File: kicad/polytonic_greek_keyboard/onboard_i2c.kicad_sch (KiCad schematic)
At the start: 13 parts, among them Q1 S8050, U2 PCF8574T

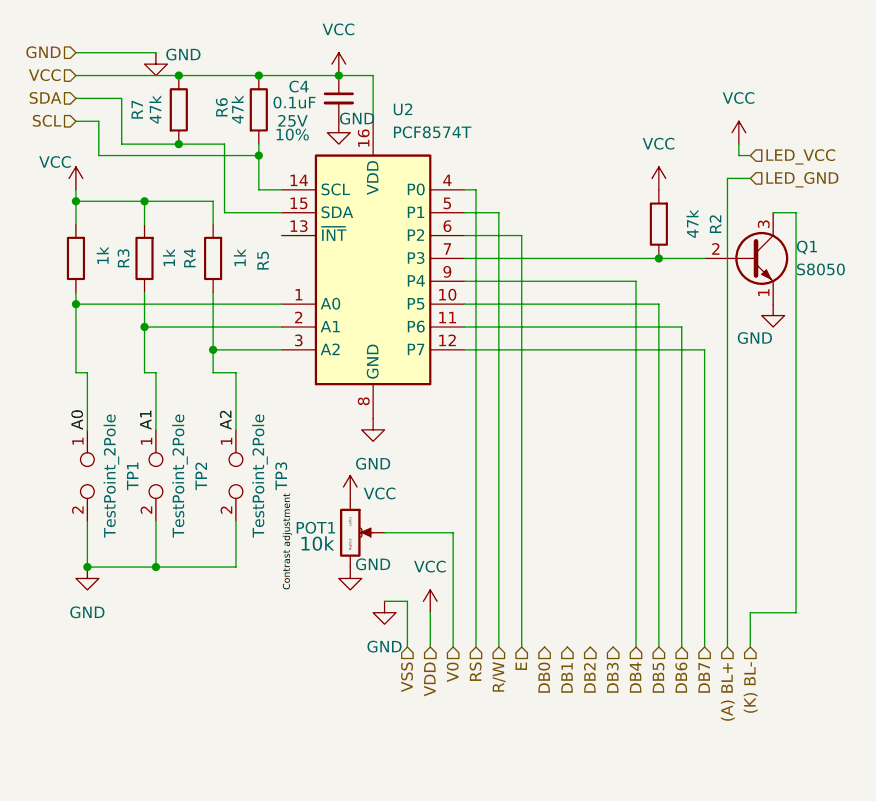
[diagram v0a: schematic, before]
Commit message: [ADD] a more structured approach of the pcb in a way that won't overload the esp32 that is running it
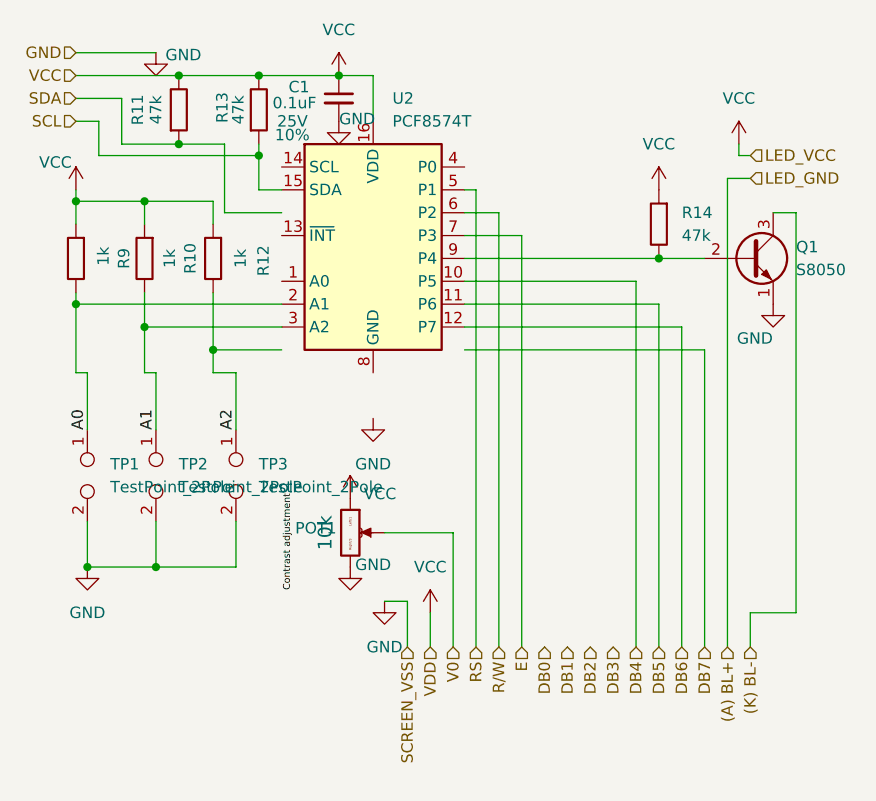
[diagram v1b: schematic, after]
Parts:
- POT1: footprint PCM_Potentiometer_THT_US_AKL:Potentiometer_Alps_RK09L_Single_Vertical -> Misc:Potentiometer_Piher_PC-16_Single_Vertical
- TP1, TP2, TP3: footprint Pin_Headers:Pin_Header_Straight_2x01_Pitch2.00mm_SMD -> Misc:TestPoint_2Pads_Pitch5.08mm_Drill1.3mm
- renumbered C4 to C1, R4 to R10, R7 to R11, R5 to R12, R6 to R13, R2 to R14, R3 to R9
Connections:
- net A0: now also U2.2 (A1); no longer U2.1 (A0)
- net A1: now also U2.3 (A2); no longer U2.2 (A1)
- net A2: no longer U2.3 (A2)
- net DB4: now also U2.10 (P5); no longer U2.9 (P4)
- net DB5: now also U2.11 (P6); no longer U2.10 (P5)
- net DB6: now also U2.12 (P7); no longer U2.11 (P6)
- net DB7: no longer U2.12 (P7)
- net E: now also U2.7 (P3); no longer U2.6 (P2)
- net GND: no longer U2.8 (GND)
- net RS: now also U2.5 (P1); no longer U2.4 (P0)
- net R/W: now also U2.6 (P2); no longer U2.5 (P1)
- net SCL: now also U2.15 (SDA); no longer U2.14 (SCL)
- net SDA: no longer U2.15 (SDA)
- net at Q1.2 (B), R14.2: now also U2.9 (P4); no longer U2.7 (P3)
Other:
- moved on the sheet: U2

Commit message: [UPDATE] the board desing, [FIX] connection issues
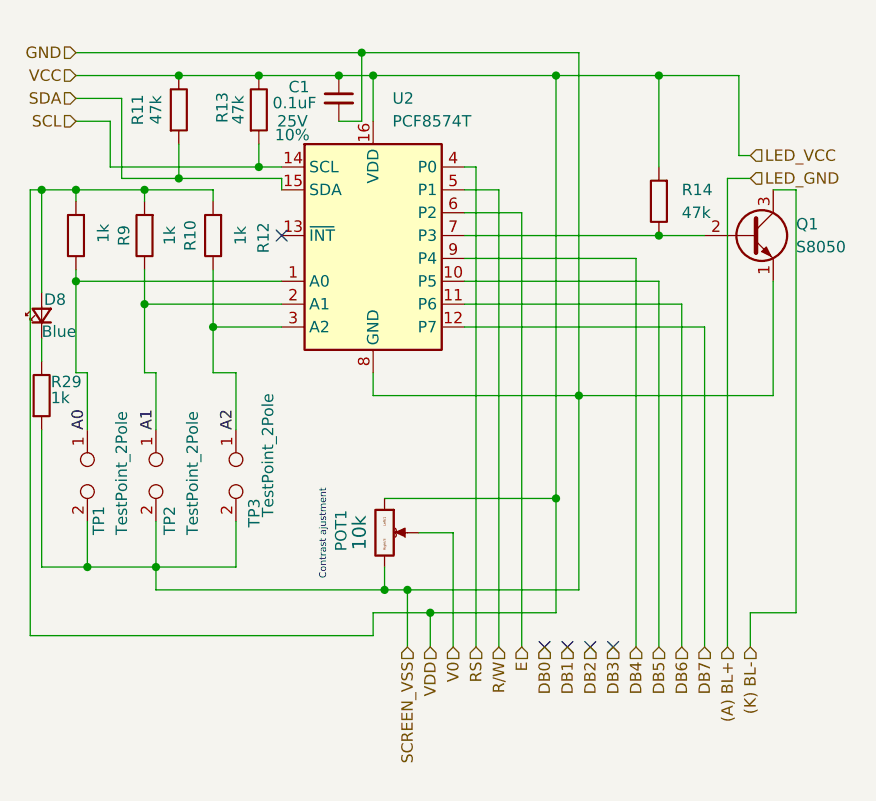
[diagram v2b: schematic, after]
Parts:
- added D8: Blue, PCM_SparkFun-LED:LED_1206_3216Metric_Blue, symbol PCM_SparkFun-LED:LED_Blue_1206
- added R29: 1k, Resistor_THT:R_Axial_DIN0207_L6.3mm_D2.5mm_P10.16mm_Horizontal, symbol PCM_SL_Resistors:1k
- POT1: footprint Misc:Potentiometer_Piher_PC-16_Single_Vertical -> Misc:Potentiometer_TT_P0915N
- TP1, TP2, TP3: footprint Misc:TestPoint_2Pads_Pitch5.08mm_Drill1.3mm -> Connector_PinHeader_2.00mm:PinHeader_1x02_P2.00mm_Horizontal
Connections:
- net A0: now also U2.1 (A0); no longer U2.2 (A1)
- net A1: now also U2.2 (A1); no longer U2.3 (A2)
- net A2: now also U2.3 (A2)
- net DB4: now also U2.9 (P4); no longer U2.10 (P5)
- net DB5: now also U2.10 (P5); no longer U2.11 (P6)
- net DB6: now also U2.11 (P6); no longer U2.12 (P7)
- net DB7: now also U2.12 (P7)
- net E: now also U2.6 (P2); no longer U2.7 (P3)
- net GND: now also U2.8 (GND), R29.1
- net RS: now also U2.4 (P0); no longer U2.5 (P1)
- net R/W: now also U2.5 (P1); no longer U2.6 (P2)
- net SCL: now also U2.14 (SCL); no longer U2.15 (SDA)
- net SDA: now also U2.15 (SDA)
- net at Q1.2 (B), R14.2: now also U2.7 (P3); no longer U2.9 (P4)
- net VCC renamed LED_VCC
- net LED_VCC: now also D8.2 (A)
- new net: D8.1 (K), R29.2
- no-connect marks 0 -> 5
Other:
- note added: "Contrast ajustment"
- moved on the sheet: POT1, Q1, R10, R12, R14, R9

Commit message: [UPDATE] the desing to fit on two separate pcbs
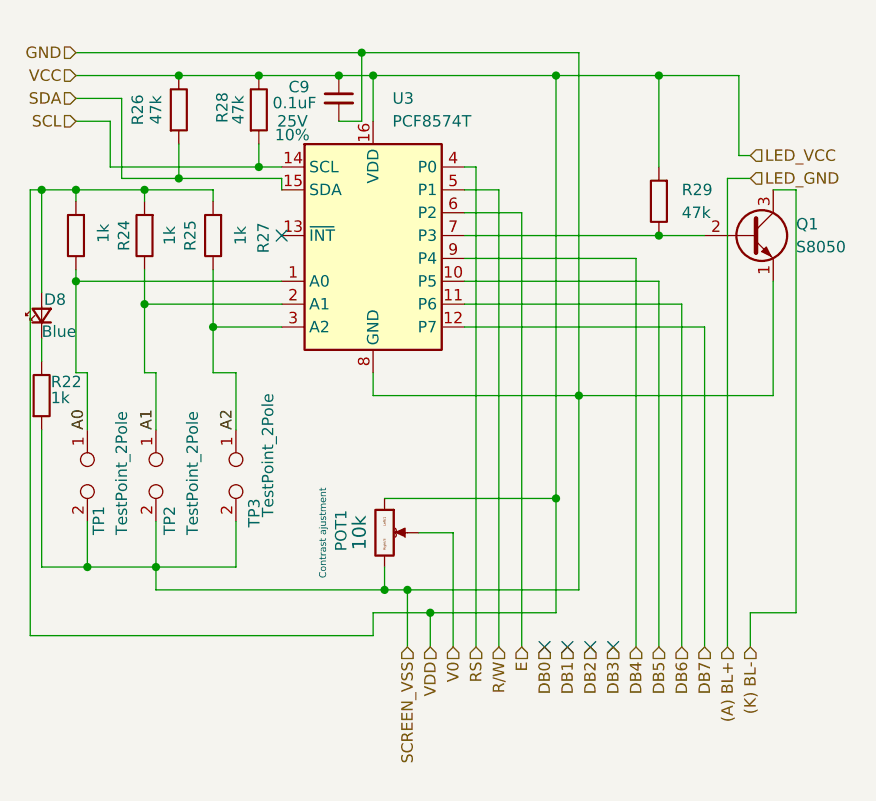
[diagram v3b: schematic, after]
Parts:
- renumbered C1 to C9, R29 to R22, R9 to R24, R10 to R25, R11 to R26, R12 to R27, R13 to R28, R14 to R29, U2 to U3
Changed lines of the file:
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@@
 		)
 		(instances
-			(project ""
-				(path "/cbe25a1b-6c02-43c2-9ff9-ba274c7cf6a2/b9347469-4bb2-4648-b4dc-d6f3187000d0/79c338a4-4a9b-4797-93e1-f6bef1aecfbc"
+			(project "polytonic_greek_keyboard"
+				(path "/cbe25a1b-6c02-43c2-9ff9-ba274c7cf6a2/8498b325-11fd-4b20-a704-75ec3d8987ef/ec54e47a-8e8b-4416-b579-fc6e7c329b94/79c338a4-4a9b-4797-93e1-f6bef1aecfbc"
 					(reference "POT1")
 					(unit 1)
@@
 		(on_board yes)
 		(dnp no)
-		(property "Reference" "C1"
+		(property "Reference" "C9"
 			(at 42.672 17.78 0)
 			(effects
@@
 		)
 		(instances
-			(project ""
-				(path "/cbe25a1b-6c02-43c2-9ff9-ba274c7cf6a2/b9347469-4bb2-4648-b4dc-d6f3187000d0/79c338a4-4a9b-4797-93e1-f6bef1aecfbc"
-					(reference "C1")
+			(project "polytonic_greek_keyboard"
+				(path "/cbe25a1b-6c02-43c2-9ff9-ba274c7cf6a2/8498b325-11fd-4b20-a704-75ec3d8987ef/ec54e47a-8e8b-4416-b579-fc6e7c329b94/79c338a4-4a9b-4797-93e1-f6bef1aecfbc"
+					(reference "C9")
 					(unit 1)
 				)
@@
 		(on_board yes)
 		(dnp no)
-		(property "Reference" "R12"
+		(property "Reference" "R27"
 			(at 39.878 34.544 0)
 			(effects
@@
 		(instances
 			(project "polytonic_greek_keyboard"
-				(path "/cbe25a1b-6c02-43c2-9ff9-ba274c7cf6a2/b9347469-4bb2-4648-b4dc-d6f3187000d0/79c338a4-4a9b-4797-93e1-f6bef1aecfbc"
-					(reference "R12")
+				(path "/cbe25a1b-6c02-43c2-9ff9-ba274c7cf6a2/8498b325-11fd-4b20-a704-75ec3d8987ef/ec54e47a-8e8b-4416-b579-fc6e7c329b94/79c338a4-4a9b-4797-93e1-f6bef1aecfbc"
+					(reference "R27")
 					(unit 1)
 				)
@@
 		(on_board yes)
 		(dnp no)
-		(property "Reference" "R9"
+		(property "Reference" "R24"
 			(at 24.384 34.29 0)
 			(effects
@@
 		)
 		(instances
-			(project ""
-				(path "/cbe25a1b-6c02-43c2-9ff9-ba274c7cf6a2/b9347469-4bb2-4648-b4dc-d6f3187000d0/79c338a4-4a9b-4797-93e1-f6bef1aecfbc"
-					(reference "R9")
+			(project "polytonic_greek_keyboard"
+				(path "/cbe25a1b-6c02-43c2-9ff9-ba274c7cf6a2/8498b325-11fd-4b20-a704-75ec3d8987ef/ec54e47a-8e8b-4416-b579-fc6e7c329b94/79c338a4-4a9b-4797-93e1-f6bef1aecfbc"
+					(reference "R24")
 					(unit 1)
 				)
@@
 		)
 		(instances
-			(project ""
-				(path "/cbe25a1b-6c02-43c2-9ff9-ba274c7cf6a2/b9347469-4bb2-4648-b4dc-d6f3187000d0/79c338a4-4a9b-4797-93e1-f6bef1aecfbc"
+			(project "polytonic_greek_keyboard"
+				(path "/cbe25a1b-6c02-43c2-9ff9-ba274c7cf6a2/8498b325-11fd-4b20-a704-75ec3d8987ef/ec54e47a-8e8b-4416-b579-fc6e7c329b94/79c338a4-4a9b-4797-93e1-f6bef1aecfbc"
 					(reference "Q1")
 					(unit 1)
@@
 		)
 		(instances
-			(project ""
-				(path "/cbe25a1b-6c02-43c2-9ff9-ba274c7cf6a2/b9347469-4bb2-4648-b4dc-d6f3187000d0/79c338a4-4a9b-4797-93e1-f6bef1aecfbc"
+			(project "polytonic_greek_keyboard"
+				(path "/cbe25a1b-6c02-43c2-9ff9-ba274c7cf6a2/8498b325-11fd-4b20-a704-75ec3d8987ef/ec54e47a-8e8b-4416-b579-fc6e7c329b94/79c338a4-4a9b-4797-93e1-f6bef1aecfbc"
 					(reference "D8")
 					(unit 1)
@@
 		(instances
 			(project "polytonic_greek_keyboard"
-				(path "/cbe25a1b-6c02-43c2-9ff9-ba274c7cf6a2/b9347469-4bb2-4648-b4dc-d6f3187000d0/79c338a4-4a9b-4797-93e1-f6bef1aecfbc"
+				(path "/cbe25a1b-6c02-43c2-9ff9-ba274c7cf6a2/8498b325-11fd-4b20-a704-75ec3d8987ef/ec54e47a-8e8b-4416-b579-fc6e7c329b94/79c338a4-4a9b-4797-93e1-f6bef1aecfbc"
 					(reference "TP3")
 					(unit 1)
@@
 		(instances
 			(project "polytonic_greek_keyboard"
-				(path "/cbe25a1b-6c02-43c2-9ff9-ba274c7cf6a2/b9347469-4bb2-4648-b4dc-d6f3187000d0/79c338a4-4a9b-4797-93e1-f6bef1aecfbc"
+				(path "/cbe25a1b-6c02-43c2-9ff9-ba274c7cf6a2/8498b325-11fd-4b20-a704-75ec3d8987ef/ec54e47a-8e8b-4416-b579-fc6e7c329b94/79c338a4-4a9b-4797-93e1-f6bef1aecfbc"
 					(reference "TP2")
 					(unit 1)
@@
 		(on_board yes)
 		(dnp no)
-		(property "Reference" "R11"
+		(property "Reference" "R26"
 			(at 25.908 20.32 0)
 			(effects
@@
 		(instances
 			(project "polytonic_greek_keyboard"
-				(path "/cbe25a1b-6c02-43c2-9ff9-ba274c7cf6a2/b9347469-4bb2-4648-b4dc-d6f3187000d0/79c338a4-4a9b-4797-93e1-f6bef1aecfbc"
-					(reference "R11")
+				(path "/cbe25a1b-6c02-43c2-9ff9-ba274c7cf6a2/8498b325-11fd-4b20-a704-75ec3d8987ef/ec54e47a-8e8b-4416-b579-fc6e7c329b94/79c338a4-4a9b-4797-93e1-f6bef1aecfbc"
+					(reference "R26")
 					(unit 1)
 				)
@@
 		(on_board yes)
 		(dnp no)
-		(property "Reference" "R10"
+		(property "Reference" "R25"
 			(at 31.75 34.29 0)
 			(effects
@@
 		(instances
 			(project "polytonic_greek_keyboard"
-				(path "/cbe25a1b-6c02-43c2-9ff9-ba274c7cf6a2/b9347469-4bb2-4648-b4dc-d6f3187000d0/79c338a4-4a9b-4797-93e1-f6bef1aecfbc"
-					(reference "R10")
+				(path "/cbe25a1b-6c02-43c2-9ff9-ba274c7cf6a2/8498b325-11fd-4b20-a704-75ec3d8987ef/ec54e47a-8e8b-4416-b579-fc6e7c329b94/79c338a4-4a9b-4797-93e1-f6bef1aecfbc"
+					(reference "R25")
 					(unit 1)
 				)
@@
 		(on_board yes)
 		(dnp no)
-		(property "Reference" "R13"
+		(property "Reference" "R28"
 			(at 35.306 20.066 0)
 			(effects
@@
 		)
 		(instances
-			(project ""
-				(path "/cbe25a1b-6c02-43c2-9ff9-ba274c7cf6a2/b9347469-4bb2-4648-b4dc-d6f3187000d0/79c338a4-4a9b-4797-93e1-f6bef1aecfbc"
-					(reference "R13")
+			(project "polytonic_greek_keyboard"
+				(path "/cbe25a1b-6c02-43c2-9ff9-ba274c7cf6a2/8498b325-11fd-4b20-a704-75ec3d8987ef/ec54e47a-8e8b-4416-b579-fc6e7c329b94/79c338a4-4a9b-4797-93e1-f6bef1aecfbc"
+					(reference "R28")
 					(unit 1)
 				)
@@
 		(dnp no)
 		(fields_autoplaced yes)
-		(property "Reference" "U2"
+		(property "Reference" "U3"
 			(at 54.2133 19.05 0)
 			(effects
@@
 		)
 		(instances
-			(project ""
-				(path "/cbe25a1b-6c02-43c2-9ff9-ba274c7cf6a2/b9347469-4bb2-4648-b4dc-d6f3187000d0/79c338a4-4a9b-4797-93e1-f6bef1aecfbc"
-					(reference "U2")
+			(project "polytonic_greek_keyboard"
+				(path "/cbe25a1b-6c02-43c2-9ff9-ba274c7cf6a2/8498b325-11fd-4b20-a704-75ec3d8987ef/ec54e47a-8e8b-4416-b579-fc6e7c329b94/79c338a4-4a9b-4797-93e1-f6bef1aecfbc"
+					(reference "U3")
 					(unit 1)
 				)
@@
 		(dnp no)
 		(fields_autoplaced yes)
-		(property "Reference" "R14"
+		(property "Reference" "R29"
 			(at 86.36 29.2099 90)
 			(effects
@@
 		)
 		(instances
-			(project ""
-				(path "/cbe25a1b-6c02-43c2-9ff9-ba274c7cf6a2/b9347469-4bb2-4648-b4dc-d6f3187000d0/79c338a4-4a9b-4797-93e1-f6bef1aecfbc"
-					(reference "R14")
+			(project "polytonic_greek_keyboard"
+				(path "/cbe25a1b-6c02-43c2-9ff9-ba274c7cf6a2/8498b325-11fd-4b20-a704-75ec3d8987ef/ec54e47a-8e8b-4416-b579-fc6e7c329b94/79c338a4-4a9b-4797-93e1-f6bef1aecfbc"
+					(reference "R29")
 					(unit 1)
 				)
@@
 		)
 		(instances
-			(project ""
-				(path "/cbe25a1b-6c02-43c2-9ff9-ba274c7cf6a2/b9347469-4bb2-4648-b4dc-d6f3187000d0/79c338a4-4a9b-4797-93e1-f6bef1aecfbc"
+			(project "polytonic_greek_keyboard"
+				(path "/cbe25a1b-6c02-43c2-9ff9-ba274c7cf6a2/8498b325-11fd-4b20-a704-75ec3d8987ef/ec54e47a-8e8b-4416-b579-fc6e7c329b94/79c338a4-4a9b-4797-93e1-f6bef1aecfbc"
 					(reference "TP1")
 					(unit 1)
@@
 		(on_board yes)
 		(dnp no)
-		(property "Reference" "R29"
+		(property "Reference" "R22"
 			(at 16.256 50.546 90)
 			(effects
@@
 		)
 		(instances
-			(project ""
-				(path "/cbe25a1b-6c02-43c2-9ff9-ba274c7cf6a2/b9347469-4bb2-4648-b4dc-d6f3187000d0/79c338a4-4a9b-4797-93e1-f6bef1aecfbc"
-					(reference "R29")
-					(unit 1)
-				)
+			(project "polytonic_greek_keyboard"
+				(path "/cbe25a1b-6c02-43c2-9ff9-ba274c7cf6a2/8498b325-11fd-4b20-a704-75ec3d8987ef/ec54e47a-8e8b-4416-b579-fc6e7c329b94/79c338a4-4a9b-4797-93e1-f6bef1aecfbc"
+					(reference "R22")
+					(unit 1)
+				)

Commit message: [UPDATE] anotation issues
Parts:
- renumbered C9 to C1, D8 to D1, R22 to R1, R24 to R2, R25 to R3, R26 to R4, R27 to R5, R28 to R6, R29 to R7, U3 to U1
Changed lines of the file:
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@@
 		(on_board yes)
 		(dnp no)
-		(property "Reference" "C9"
+		(property "Reference" "C1"
 			(at 42.672 17.78 0)
 			(effects
@@
 			(project "polytonic_greek_keyboard"
 				(path "/cbe25a1b-6c02-43c2-9ff9-ba274c7cf6a2/8498b325-11fd-4b20-a704-75ec3d8987ef/ec54e47a-8e8b-4416-b579-fc6e7c329b94/79c338a4-4a9b-4797-93e1-f6bef1aecfbc"
-					(reference "C9")
+					(reference "C1")
 					(unit 1)
 				)
@@
 		(on_board yes)
 		(dnp no)
-		(property "Reference" "R27"
+		(property "Reference" "R5"
 			(at 39.878 34.544 0)
 			(effects
@@
 			(project "polytonic_greek_keyboard"
 				(path "/cbe25a1b-6c02-43c2-9ff9-ba274c7cf6a2/8498b325-11fd-4b20-a704-75ec3d8987ef/ec54e47a-8e8b-4416-b579-fc6e7c329b94/79c338a4-4a9b-4797-93e1-f6bef1aecfbc"
-					(reference "R27")
+					(reference "R5")
 					(unit 1)
 				)
@@
 		(on_board yes)
 		(dnp no)
-		(property "Reference" "R24"
+		(property "Reference" "R2"
 			(at 24.384 34.29 0)
 			(effects
@@
 			(project "polytonic_greek_keyboard"
 				(path "/cbe25a1b-6c02-43c2-9ff9-ba274c7cf6a2/8498b325-11fd-4b20-a704-75ec3d8987ef/ec54e47a-8e8b-4416-b579-fc6e7c329b94/79c338a4-4a9b-4797-93e1-f6bef1aecfbc"
-					(reference "R24")
+					(reference "R2")
 					(unit 1)
 				)
@@
 		(on_board yes)
 		(dnp no)
-		(property "Reference" "D8"
+		(property "Reference" "D1"
 			(at 15.494 41.402 90)
 			(effects
@@
 			(project "polytonic_greek_keyboard"
 				(path "/cbe25a1b-6c02-43c2-9ff9-ba274c7cf6a2/8498b325-11fd-4b20-a704-75ec3d8987ef/ec54e47a-8e8b-4416-b579-fc6e7c329b94/79c338a4-4a9b-4797-93e1-f6bef1aecfbc"
-					(reference "D8")
+					(reference "D1")
 					(unit 1)
 				)
@@
 		(on_board yes)
 		(dnp no)
-		(property "Reference" "R26"
+		(property "Reference" "R4"
 			(at 25.908 20.32 0)
 			(effects
@@
 			(project "polytonic_greek_keyboard"
 				(path "/cbe25a1b-6c02-43c2-9ff9-ba274c7cf6a2/8498b325-11fd-4b20-a704-75ec3d8987ef/ec54e47a-8e8b-4416-b579-fc6e7c329b94/79c338a4-4a9b-4797-93e1-f6bef1aecfbc"
-					(reference "R26")
+					(reference "R4")
 					(unit 1)
 				)
@@
 		(on_board yes)
 		(dnp no)
-		(property "Reference" "R25"
+		(property "Reference" "R3"
 			(at 31.75 34.29 0)
 			(effects
@@
 			(project "polytonic_greek_keyboard"
 				(path "/cbe25a1b-6c02-43c2-9ff9-ba274c7cf6a2/8498b325-11fd-4b20-a704-75ec3d8987ef/ec54e47a-8e8b-4416-b579-fc6e7c329b94/79c338a4-4a9b-4797-93e1-f6bef1aecfbc"
-					(reference "R25")
+					(reference "R3")
 					(unit 1)
 				)
@@
 		(on_board yes)
 		(dnp no)
-		(property "Reference" "R28"
+		(property "Reference" "R6"
 			(at 35.306 20.066 0)
 			(effects
@@
 			(project "polytonic_greek_keyboard"
 				(path "/cbe25a1b-6c02-43c2-9ff9-ba274c7cf6a2/8498b325-11fd-4b20-a704-75ec3d8987ef/ec54e47a-8e8b-4416-b579-fc6e7c329b94/79c338a4-4a9b-4797-93e1-f6bef1aecfbc"
-					(reference "R28")
+					(reference "R6")
 					(unit 1)
 				)
@@
 		(dnp no)
 		(fields_autoplaced yes)
-		(property "Reference" "U3"
+		(property "Reference" "U1"
 			(at 54.2133 19.05 0)
 			(effects
@@
 			(project "polytonic_greek_keyboard"
 				(path "/cbe25a1b-6c02-43c2-9ff9-ba274c7cf6a2/8498b325-11fd-4b20-a704-75ec3d8987ef/ec54e47a-8e8b-4416-b579-fc6e7c329b94/79c338a4-4a9b-4797-93e1-f6bef1aecfbc"
-					(reference "U3")
+					(reference "U1")
 					(unit 1)
 				)
@@
 		(dnp no)
 		(fields_autoplaced yes)
-		(property "Reference" "R29"
+		(property "Reference" "R7"
 			(at 86.36 29.2099 90)
 			(effects
@@
 			(project "polytonic_greek_keyboard"
 				(path "/cbe25a1b-6c02-43c2-9ff9-ba274c7cf6a2/8498b325-11fd-4b20-a704-75ec3d8987ef/ec54e47a-8e8b-4416-b579-fc6e7c329b94/79c338a4-4a9b-4797-93e1-f6bef1aecfbc"
-					(reference "R29")
+					(reference "R7")
 					(unit 1)
 				)
@@
 		(on_board yes)
 		(dnp no)
-		(property "Reference" "R22"
+		(property "Reference" "R1"
 			(at 16.256 50.546 90)
 			(effects
@@
 			(project "polytonic_greek_keyboard"
 				(path "/cbe25a1b-6c02-43c2-9ff9-ba274c7cf6a2/8498b325-11fd-4b20-a704-75ec3d8987ef/ec54e47a-8e8b-4416-b579-fc6e7c329b94/79c338a4-4a9b-4797-93e1-f6bef1aecfbc"
-					(reference "R22")
-					(unit 1)
-				)
+					(reference "R1")
+					(unit 1)
+				)

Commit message: [UPDATE] the final merged version of the schematic before splitting into two separate kicad projects
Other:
- company: (none) -> Henry's Software House
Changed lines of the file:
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@@
 		(title "Intergrated I²C board")
 		(date "2025-09-11")
-		(rev "0")
+		(rev "1 - do not edit connector pin layout.")
+		(company "Henry's Software House")
 		(comment 1 "This is an attempt at recreating the I²C chip used in lcd segment displays to free up data lines on the controlers.")
 	)
